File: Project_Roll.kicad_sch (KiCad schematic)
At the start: 69 parts, among them J1 TB002-500-02BE, J10 Conn_01x04, J11 Conn_01x04, J12 Conn_01x02, J13 TB002-500-02BE, J14 TB002-500-02BE, J15 TB002-500-02BE, J16 TB002-500-02BE, J2 TB002-500-02BE, J3 TB002-500-02BE, J4 TB002-500-02BE, J5 TB002-500-02BE, J6 Conn_01x05, J7 Conn_01x05, J8 Conn_01x04, J9 Conn_01x04, Q1 IRFS7430TRLPBF, U1 AP62300TWU, U2 GY-521, U3 ESP32-DEVKIT-V1

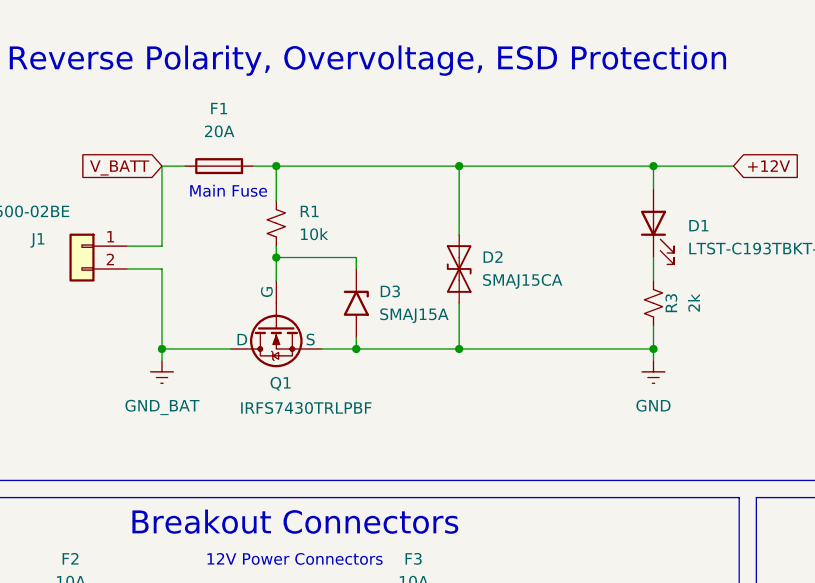
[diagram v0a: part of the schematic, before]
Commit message: TVS Diode fix and layout changes
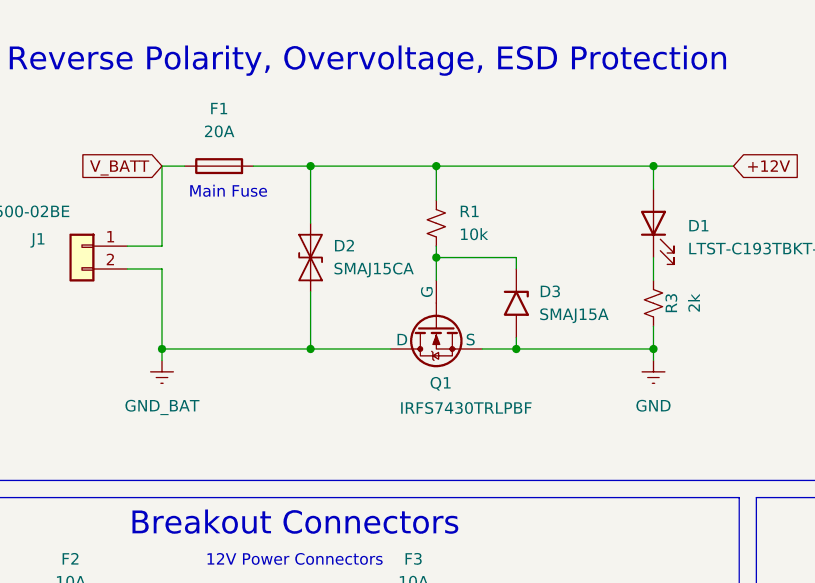
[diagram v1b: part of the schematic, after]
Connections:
- net GND: no longer D2.2 (A2)
- net GND_BAT: now also D2.2 (A2)
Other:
- moved on the sheet: D3, Q1, R1

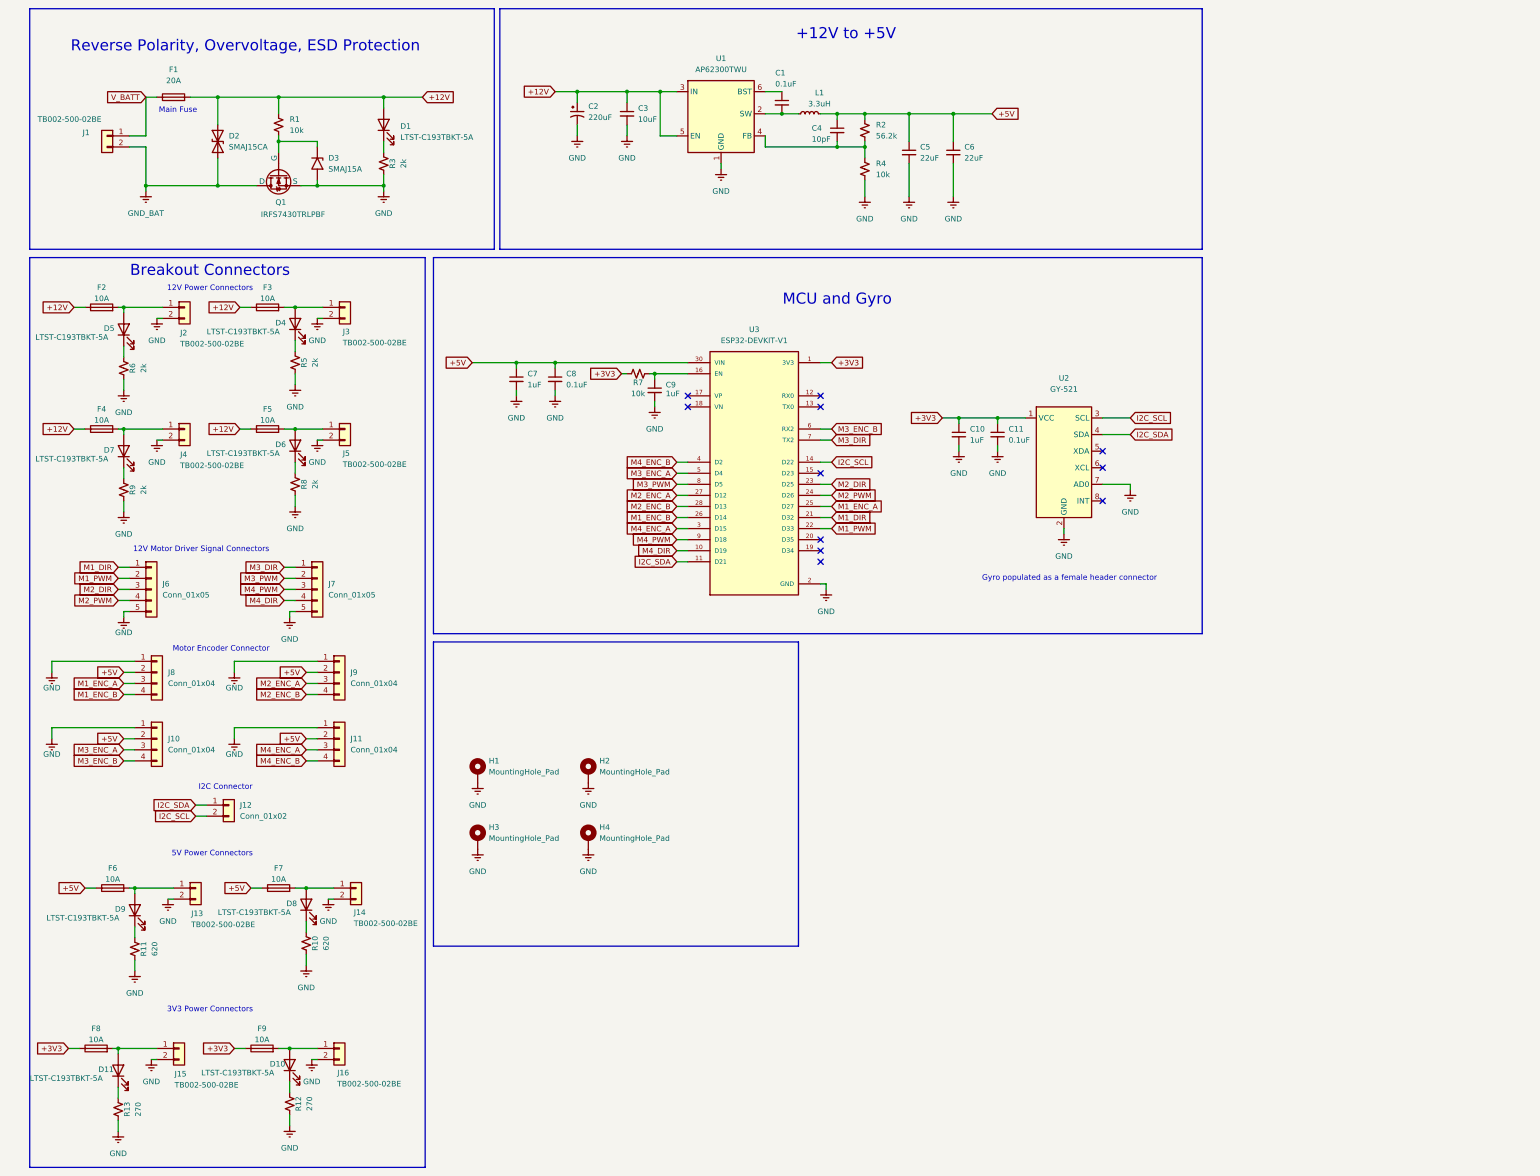
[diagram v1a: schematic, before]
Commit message: Vias for power connections
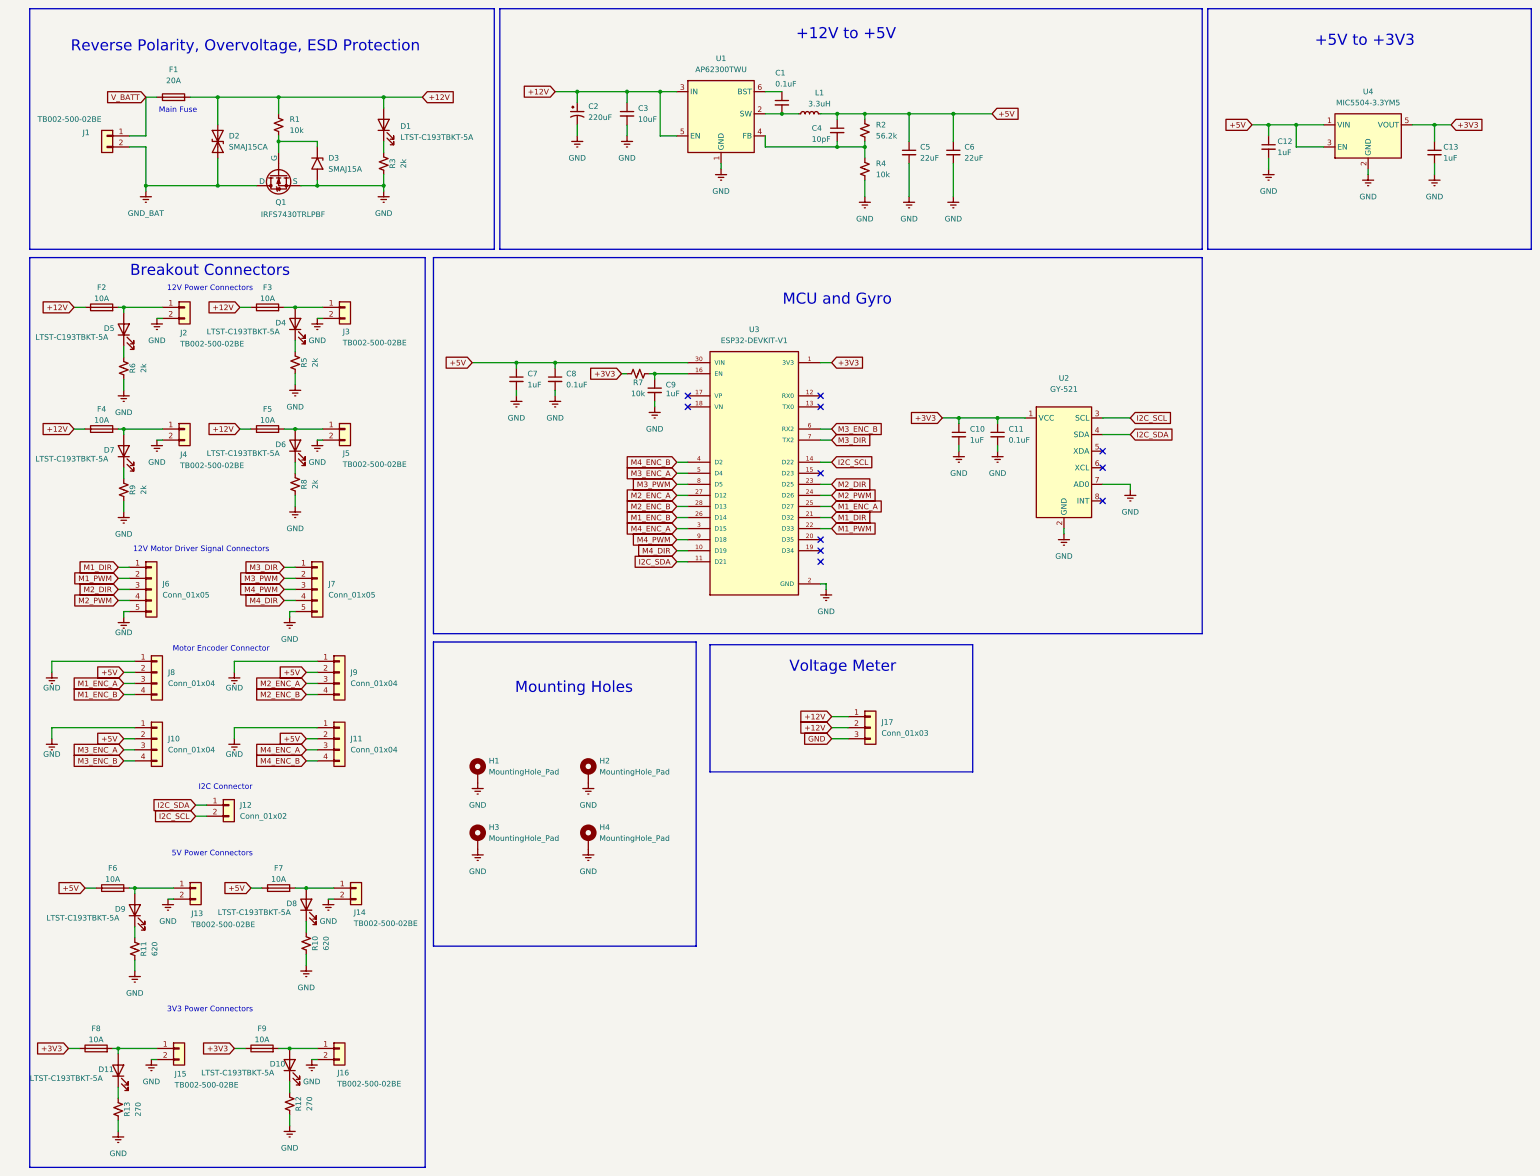
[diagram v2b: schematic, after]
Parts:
- added C12, C13: 1uF, Capacitor_SMD:C_0603_1608Metric_Pad1.08x0.95mm_HandSolder, symbol Device:C_Small
- added J17: Conn_01x03, BB8 Footprints:Voltage Meter, symbol Connector_Generic:Conn_01x03
- added U4: MIC5504-3.3YM5, Package_TO_SOT_SMD:SOT-23-5, symbol Regulator_Linear:MIC5504-3.3YM5
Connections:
- net +12V: now also J17.1 (Pin_1), J17.2 (Pin_2)
- net +3V3: now also C13.1, U4.5 (VOUT)
- net +5V: now also C12.1, U4.1 (VIN), U4.3 (EN)
- net GND: now also C12.2, C13.2, J17.3 (Pin_3), U4.2 (GND)
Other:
- note added: "+5V to +3V3"
- note added: "Mounting Holes"
- note added: "Voltage Meter"
- note removed: "Gyro populated as a female header connector"

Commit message: fixed 5v fill
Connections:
- net +3V3: no longer U3.1 (3V3)
- no-connect marks 11 -> 12
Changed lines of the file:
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@@
+	)
+	(no_connect
+		(at 195.58 95.25)
 	)
 	(no_connect
@@
 		(pts
 			(xy 29.21 215.9) (xy 26.67 215.9)
-		)
-		(stroke
-			(width 0)
-			(type default)
-		)
-	)
-	(wire
-		(pts
-			(xy 195.58 95.25) (xy 198.12 95.25)
 		)
 		(stroke
@@
 			)
 		)
-	)
-	(global_label "+3V3"
-		(shape input)
-		(at 198.12 95.25 0)
-		(fields_autoplaced yes)
-		(effects
-			(font
-				(size 1.27 1.27)
-			)
-			(justify left)
-		)
-		(property "Intersheetrefs" "${INTERSHEET_REFS}"
-			(at 206.1852 95.25 0)
-			(hide yes)
-			(show_name no)
-			(do_not_autoplace no)
-			(effects
-				(font
-					(size 1.27 1.27)
-				)
-				(justify left)
-			)
-		)

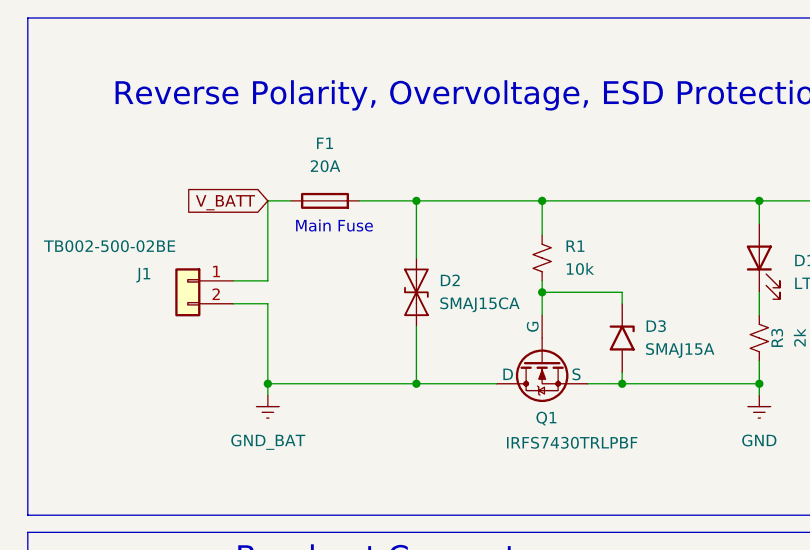
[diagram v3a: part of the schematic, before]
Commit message: cleaned up fills
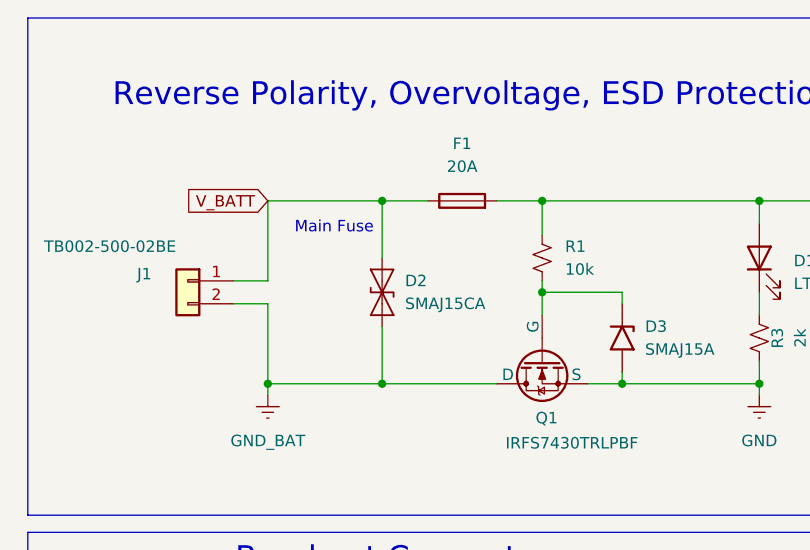
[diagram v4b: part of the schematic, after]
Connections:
- net +12V: no longer D2.1 (A1)
- net V_BATT: now also D2.1 (A1)
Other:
- moved on the sheet: D2
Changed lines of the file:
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@@
 	)
 	(junction
-		(at 57.15 54.61)
+		(at 40.64 54.61)
 		(diameter 0)
 		(color 0 0 0 0)
 	)
 	(junction
-		(at 40.64 54.61)
+		(at 53.34 54.61)
 		(diameter 0)
 		(color 0 0 0 0)
@@
 	)
 	(junction
+		(at 53.34 34.29)
+		(diameter 0)
+		(color 0 0 0 0)
+	)
+	(junction
 		(at 158.75 33.02)
 		(diameter 0)
@@
 	)
 	(junction
-		(at 57.15 34.29)
-		(diameter 0)
-		(color 0 0 0 0)
-	)
-	(junction
 		(at 35.56 82.55)
 		(diameter 0)
@@
 	(wire
 		(pts
+			(xy 53.34 34.29) (xy 58.42 34.29)
+		)
+		(stroke
+			(width 0)
+			(type default)
+		)
+	)
+	(wire
+		(pts
 			(xy 199.39 45.72) (xy 205.74 45.72)
 		)
@@
 	(wire
 		(pts
-			(xy 57.15 34.29) (xy 57.15 40.64)
+			(xy 53.34 34.29) (xy 53.34 40.64)
 		)
 		(stroke
@@
 	(wire
 		(pts
+			(xy 53.34 54.61) (xy 66.04 54.61)
+		)
+		(stroke
+			(width 0)
+			(type default)
+		)
+	)
+	(wire
+		(pts
 			(xy 72.39 147.32) (xy 74.93 147.32)
 		)
@@
 	(wire
 		(pts
-			(xy 40.64 34.29) (xy 43.18 34.29)
+			(xy 40.64 34.29) (xy 53.34 34.29)
 		)
 		(stroke
@@
 	(wire
 		(pts
-			(xy 40.64 54.61) (xy 57.15 54.61)
+			(xy 40.64 54.61) (xy 53.34 54.61)
 		)
 		(stroke
@@
 	(wire
 		(pts
-			(xy 57.15 54.61) (xy 66.04 54.61)
-		)
-		(stroke
-			(width 0)
-			(type default)
-		)
-	)
-	(wire
-		(pts
 			(xy 199.39 45.72) (xy 199.39 44.45)
 		)
@@
 	(wire
 		(pts
-			(xy 50.8 34.29) (xy 57.15 34.29)
-		)
-		(stroke
-			(width 0)
-			(type default)
-		)
-	)
-	(wire
-		(pts
 			(xy 35.56 184.15) (xy 38.1 184.15)
 		)
@@
 	(wire
 		(pts
-			(xy 43.18 113.03) (xy 44.45 113.03)
+			(xy 66.04 34.29) (xy 71.12 34.29)
 		)
 		(stroke
@@
 	(wire
 		(pts
-			(xy 60.96 179.07) (xy 60.96 181.61)
+			(xy 43.18 113.03) (xy 44.45 113.03)
 		)
 		(stroke
@@
 	(wire
 		(pts
-			(xy 304.8 45.72) (xy 304.8 40.64)
+			(xy 60.96 179.07) (xy 60.96 181.61)
 		)
 		(stroke
@@
 	(wire
 		(pts
-			(xy 57.15 34.29) (xy 71.12 34.29)
+			(xy 304.8 45.72) (xy 304.8 40.64)
 		)
 		(stroke
@@
 	(wire
 		(pts
-			(xy 57.15 48.26) (xy 57.15 54.61)
+			(xy 53.34 48.26) (xy 53.34 54.61)
 		)
 		(stroke
@@
 	)
 	(symbol
-		(lib_id "Device:Fuse")
-		(at 46.99 34.29 90)
-		(unit 1)
-		(body_style 1)
-		(exclude_from_sim no)
-		(in_bom yes)
-		(on_board yes)
-		(in_pos_files yes)
-		(dnp no)
-		(fields_autoplaced yes)
-		(property "Reference" "F1"
-			(at 46.99 27.94 90)
-			(show_name no)
-			(do_not_autoplace no)
-			(effects
-				(font
-					(size 1.27 1.27)
-				)
-			)
-		)
-		(property "Value" "20A"
-			(at 46.99 30.48 90)
-			(show_name no)
-			(do_not_autoplace no)
-			(effects
-				(font
-					(size 1.27 1.27)
-				)
-			)
-		)
-		(property "Footprint" "BB8 Footprints:CONN_3557-2_KEY"
-			(at 46.99 36.068 90)
-			(hide yes)
-			(show_name no)
-			(do_not_autoplace no)
-			(effects
-				(font
-					(size 1.27 1.27)
-				)
-			)
-		)
-		(property "Datasheet" ""
-			(at 46.99 34.29 0)
-			(hide yes)
-			(show_name no)
-			(do_not_autoplace no)
-			(effects
-				(font
-					(size 1.27 1.27)
-				)
-			)
-		)
-		(property "Description" "Fuse"
-			(at 46.99 34.29 0)
-			(hide yes)
-			(show_name no)
-			(do_not_autoplace no)
-			(effects
-				(font
-					(size 1.27 1.27)
-				)
-			)
-		)
-		(pin "2"
-		)
-		(pin "1"
-		)
-		(instances
-			(project "Project_Roll"
-				(path "/9177cfca-6009-48b2-9448-13eb174bc496"
-					(reference "F1")
-					(unit 1)
-				)
-			)
-		)
-	)
-	(symbol
 		(lib_id "BB8 Symbols:GY-521")
 		(at 251.46 115.57 0)
@@
 	)
 	(symbol
+		(lib_id "Device:Fuse")
+		(at 62.23 34.29 90)
+		(unit 1)
+		(body_style 1)
+		(exclude_from_sim no)
+		(in_bom yes)
+		(on_board yes)
+		(in_pos_files yes)
+		(dnp no)
+		(fields_autoplaced yes)
+		(property "Reference" "F1"
+			(at 62.23 27.94 90)
+			(show_name no)
+			(do_not_autoplace no)
+			(effects
+				(font
+					(size 1.27 1.27)
+				)
+			)
+		)
+		(property "Value" "20A"
+			(at 62.23 30.48 90)
+			(show_name no)
+			(do_not_autoplace no)
+			(effects
+				(font
+					(size 1.27 1.27)
+				)
+			)
+		)
+		(property "Footprint" "BB8 Footprints:CONN_3557-2_KEY"
+			(at 62.23 36.068 90)
+			(hide yes)
+			(show_name no)
+			(do_not_autoplace no)
+			(effects
+				(font
+					(size 1.27 1.27)
+				)
+			)
+		)
+		(property "Datasheet" ""
+			(at 62.23 34.29 0)
+			(hide yes)
+			(show_name no)
+			(do_not_autoplace no)
+			(effects
+				(font
+					(size 1.27 1.27)
+				)
+			)
+		)
+		(property "Description" "Fuse"
+			(at 62.23 34.29 0)
+			(hide yes)
+			(show_name no)
+			(do_not_autoplace no)
+			(effects
+				(font
+					(size 1.27 1.27)
+				)
+			)
+		)
+		(pin "2"
+		)
+		(pin "1"
+		)
+		(instances
+			(project "Project_Roll"
+				(path "/9177cfca-6009-48b2-9448-13eb174bc496"
+					(reference "F1")
+					(unit 1)
+				)
+			)
+		)
+	)
+	(symbol
 		(lib_id "Connector_Generic:Conn_01x02")
 		(at 31.75 43.18 0)
@@
 	(symbol
 		(lib_id "Diode:SMAJ15CA")
-		(at 57.15 44.45 270)
+		(at 53.34 44.45 270)
 		(unit 1)
 		(body_style 1)
@@
 		(fields_autoplaced yes)
 		(property "Reference" "D2"
-			(at 59.69 43.1799 90)
+			(at 55.88 43.1799 90)
 			(show_name no)
 			(do_not_autoplace no)
@@
 		)
 		(property "Value" "SMAJ15CA"
-			(at 59.69 45.7199 90)
+			(at 55.88 45.7199 90)
 			(show_name no)
 			(do_not_autoplace no)
@@
 		)
 		(property "Footprint" "Diode_SMD:D_SMA"
-			(at 52.07 44.45 0)
+			(at 48.26 44.45 0)
 			(hide yes)
 			(show_name no)
@@
 		)
 		(property "Datasheet" "https://www.littelfuse.com/media?resourcetype=datasheets&itemid=75e32973-b177-4ee3-a0ff-cedaf1abdb93&filename=smaj-datasheet"
-			(at 57.15 44.45 0)
+			(at 53.34 44.45 0)
 			(hide yes)
 			(show_name no)
@@
 		)
 		(property "Description" "400W bidirectional Transient Voltage Suppressor, 15.0Vr, SMA(DO-214AC)"
-			(at 57.15 44.45 0)
+			(at 53.34 44.45 0)
 			(hide yes)
 			(show_name no)
